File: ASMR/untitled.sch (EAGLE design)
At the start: 22 parts, among them J1 POWER_JACKSLT

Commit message: revisi PCB
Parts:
- added C3: 100nF, rcl:C-EUC0805K
- added R4: 10k, adafruit:R-US_M0805
- added S1: (no value), switch-omron:31-XX
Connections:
- new net RST: C3.1, R4.1, S1.S, U$6.IO0
- new net SCL: RTC1.SCL1, U$6.IO22
- new net SDA: RTC1.SDA1, U$6.IO21
- net GND: now also C3.2, RTC1.GND1, S1.P
- net INT_LAN: no longer U$6.IO22
- net OUT+: now also R4.2, RTC1.VCC1
- net RST_LAN: no longer U$6.IO21
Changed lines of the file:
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@@
 <part name="X2" library="con-molex" library_urn="urn:adsk.eagle:library:165" deviceset="KK-156-2" device="" package3d_urn="urn:adsk.eagle:package:8078800/1"/>
 <part name="RTC1" library="rtc3231" deviceset="RTC3231" device=""/>
+<part name="GND3" library="supply1" library_urn="urn:adsk.eagle:library:371" deviceset="GND" device=""/>
+<part name="S1" library="switch-omron" library_urn="urn:adsk.eagle:library:377" deviceset="31-XX" device="" package3d_urn="urn:adsk.eagle:package:27487/1"/>
+<part name="C3" library="rcl" library_urn="urn:adsk.eagle:library:334" deviceset="C-EU" device="C0805K" package3d_urn="urn:adsk.eagle:package:23681/2" value="100nF"/>
+<part name="R4" library="adafruit" library_urn="urn:adsk.eagle:library:420" deviceset="R-US_" device="M0805" package3d_urn="urn:adsk.eagle:package:6240587/1" value="10k"/>
 </parts>
 <sheets>
@@
 </instance>
 <instance part="RTC1" gate="G$1" x="88.9" y="35.56" smashed="yes"/>
+<instance part="GND3" gate="1" x="109.22" y="45.72" smashed="yes" rot="R180">
+<attribute name="VALUE" x="111.76" y="48.26" size="1.778" layer="96" rot="R180"/>
+</instance>
+<instance part="S1" gate="1" x="-104.14" y="30.48" smashed="yes" rot="R270">
+<attribute name="NAME" x="-106.045" y="36.83" size="1.778" layer="95"/>
+<attribute name="VALUE" x="-100.965" y="34.29" size="1.778" layer="96"/>
+</instance>
+<instance part="C3" gate="G$1" x="-101.6" y="27.94" smashed="yes" rot="R270">
+<attribute name="NAME" x="-101.219" y="26.416" size="1.778" layer="95" rot="R270"/>
+<attribute name="VALUE" x="-106.299" y="36.576" size="1.778" layer="96" rot="R270"/>
+</instance>
+<instance part="R4" gate="G$1" x="-96.52" y="40.64" smashed="yes" rot="R90">
+<attribute name="NAME" x="-98.0186" y="36.83" size="1.778" layer="95" rot="R90"/>
+<attribute name="VALUE" x="-93.218" y="36.83" size="1.778" layer="96" rot="R90"/>
+</instance>
 </instances>
 <busses>
@@
 <wire x1="-17.78" y1="30.48" x2="-17.78" y2="53.34" width="0.1524" layer="91"/>
 <wire x1="-17.78" y1="53.34" x2="-91.44" y2="53.34" width="0.1524" layer="91"/>
-<wire x1="-91.44" y1="53.34" x2="-91.44" y2="12.7" width="0.1524" layer="91"/>
+<wire x1="-91.44" y1="53.34" x2="-91.44" y2="25.4" width="0.1524" layer="91"/>
 <junction x="-91.44" y="12.7"/>
+<pinref part="S1" gate="1" pin="P"/>
+<wire x1="-91.44" y1="25.4" x2="-91.44" y2="12.7" width="0.1524" layer="91"/>
+<wire x1="-109.22" y1="30.48" x2="-111.76" y2="30.48" width="0.1524" layer="91"/>
+<wire x1="-111.76" y1="30.48" x2="-114.3" y2="30.48" width="0.1524" layer="91"/>
+<wire x1="-114.3" y1="30.48" x2="-114.3" y2="25.4" width="0.1524" layer="91"/>
+<wire x1="-91.44" y1="25.4" x2="-114.3" y2="25.4" width="0.1524" layer="91"/>
+<junction x="-91.44" y="25.4"/>
+<pinref part="C3" gate="G$1" pin="2"/>
+<wire x1="-106.68" y1="27.94" x2="-111.76" y2="27.94" width="0.1524" layer="91"/>
+<wire x1="-111.76" y1="27.94" x2="-111.76" y2="30.48" width="0.1524" layer="91"/>
+<junction x="-111.76" y="30.48"/>
 </segment>
 <segment>
@@
 <junction x="5.08" y="152.4"/>
 </segment>
+<segment>
+<pinref part="RTC1" gate="G$1" pin="GND1"/>
+<wire x1="104.14" y1="40.64" x2="109.22" y2="40.64" width="0.1524" layer="91"/>
+<wire x1="109.22" y1="40.64" x2="109.22" y2="43.18" width="0.1524" layer="91"/>
+<pinref part="GND3" gate="1" pin="GND"/>
+</segment>
 </net>
 <net name="3V3" class="0">
@@
 <label x="-81.28" y="-40.64" size="0.8128" layer="95" xref="yes"/>
 </segment>
-<segment>
-<pinref part="U$6" gate="G$1" pin="IO22"/>
-<wire x1="-68.58" y1="2.54" x2="-73.66" y2="2.54" width="0.1524" layer="91"/>
-<label x="-73.66" y="2.54" size="1.778" layer="95" rot="R180" xref="yes"/>
-</segment>
 </net>
 <net name="SCK_HSPI" class="0">
@@
 <wire x1="-114.3" y1="-43.18" x2="-119.38" y2="-43.18" width="0.1524" layer="91"/>
 <label x="-119.38" y="-43.18" size="0.8128" layer="95" rot="R180" xref="yes"/>
-</segment>
-<segment>
-<pinref part="U$6" gate="G$1" pin="IO21"/>
-<wire x1="-68.58" y1="10.16" x2="-73.66" y2="10.16" width="0.1524" layer="91"/>
-<label x="-73.66" y="10.16" size="1.778" layer="95" rot="R180" xref="yes"/>
 </segment>
 </net>
@@
 <label x="2.54" y="139.7" size="1.778" layer="95" xref="yes"/>
 </segment>
+<segment>
+<pinref part="RTC1" gate="G$1" pin="VCC1"/>
+<wire x1="104.14" y1="38.1" x2="119.38" y2="38.1" width="0.1524" layer="91"/>
+<wire x1="119.38" y1="38.1" x2="119.38" y2="40.64" width="0.1524" layer="91"/>
+<label x="119.38" y="40.64" size="1.778" layer="95" rot="R90" xref="yes"/>
+</segment>
+<segment>
+<pinref part="R4" gate="G$1" pin="2"/>
+<wire x1="-96.52" y1="45.72" x2="-96.52" y2="48.26" width="0.1524" layer="91"/>
+<label x="-96.52" y="48.26" size="1.778" layer="95" rot="R90" xref="yes"/>
+</segment>
 </net>
 <net name="N$2" class="0">
@@
 </segment>
 </net>
+<net name="SCL" class="0">
+<segment>
+<pinref part="U$6" gate="G$1" pin="IO22"/>
+<wire x1="-68.58" y1="2.54" x2="-73.66" y2="2.54" width="0.1524" layer="91"/>
+<label x="-73.66" y="2.54" size="1.778" layer="95" rot="R180" xref="yes"/>
+</segment>
+<segment>
+<pinref part="RTC1" gate="G$1" pin="SCL1"/>
+<wire x1="104.14" y1="33.02" x2="106.68" y2="33.02" width="0.1524" layer="91"/>
+<label x="106.68" y="33.02" size="1.778" layer="95" xref="yes"/>
+</segment>
+</net>
+<net name="SDA" class="0">
+<segment>
+<pinref part="U$6" gate="G$1" pin="IO21"/>
+<wire x1="-68.58" y1="10.16" x2="-73.66" y2="10.16" width="0.1524" layer="91"/>
+<label x="-73.66" y="10.16" size="1.778" layer="95" rot="R180" xref="yes"/>
+</segment>
+<segment>
+<pinref part="RTC1" gate="G$1" pin="SDA1"/>
+<wire x1="104.14" y1="35.56" x2="106.68" y2="35.56" width="0.1524" layer="91"/>
+<label x="106.68" y="35.56" size="1.778" layer="95" xref="yes"/>
+</segment>
+</net>
+<net name="RST" class="0">
+<segment>
+<pinref part="U$6" gate="G$1" pin="IO0"/>
+<label x="-73.66" y="30.48" size="1.778" layer="95" rot="R180" xref="yes"/>
+<pinref part="S1" gate="1" pin="S"/>
+<wire x1="-99.06" y1="30.48" x2="-96.52" y2="30.48" width="0.1524" layer="91"/>
+<pinref part="C3" gate="G$1" pin="1"/>
+<wire x1="-96.52" y1="30.48" x2="-68.58" y2="30.48" width="0.1524" layer="91"/>
+<wire x1="-99.06" y1="27.94" x2="-96.52" y2="27.94" width="0.1524" layer="91"/>
+<wire x1="-96.52" y1="27.94" x2="-96.52" y2="30.48" width="0.1524" layer="91"/>
+<junction x="-96.52" y="30.48"/>
+<pinref part="R4" gate="G$1" pin="1"/>
+<wire x1="-96.52" y1="30.48" x2="-96.52" y2="35.56" width="0.1524" layer="91"/>
+</segment>
+</net>

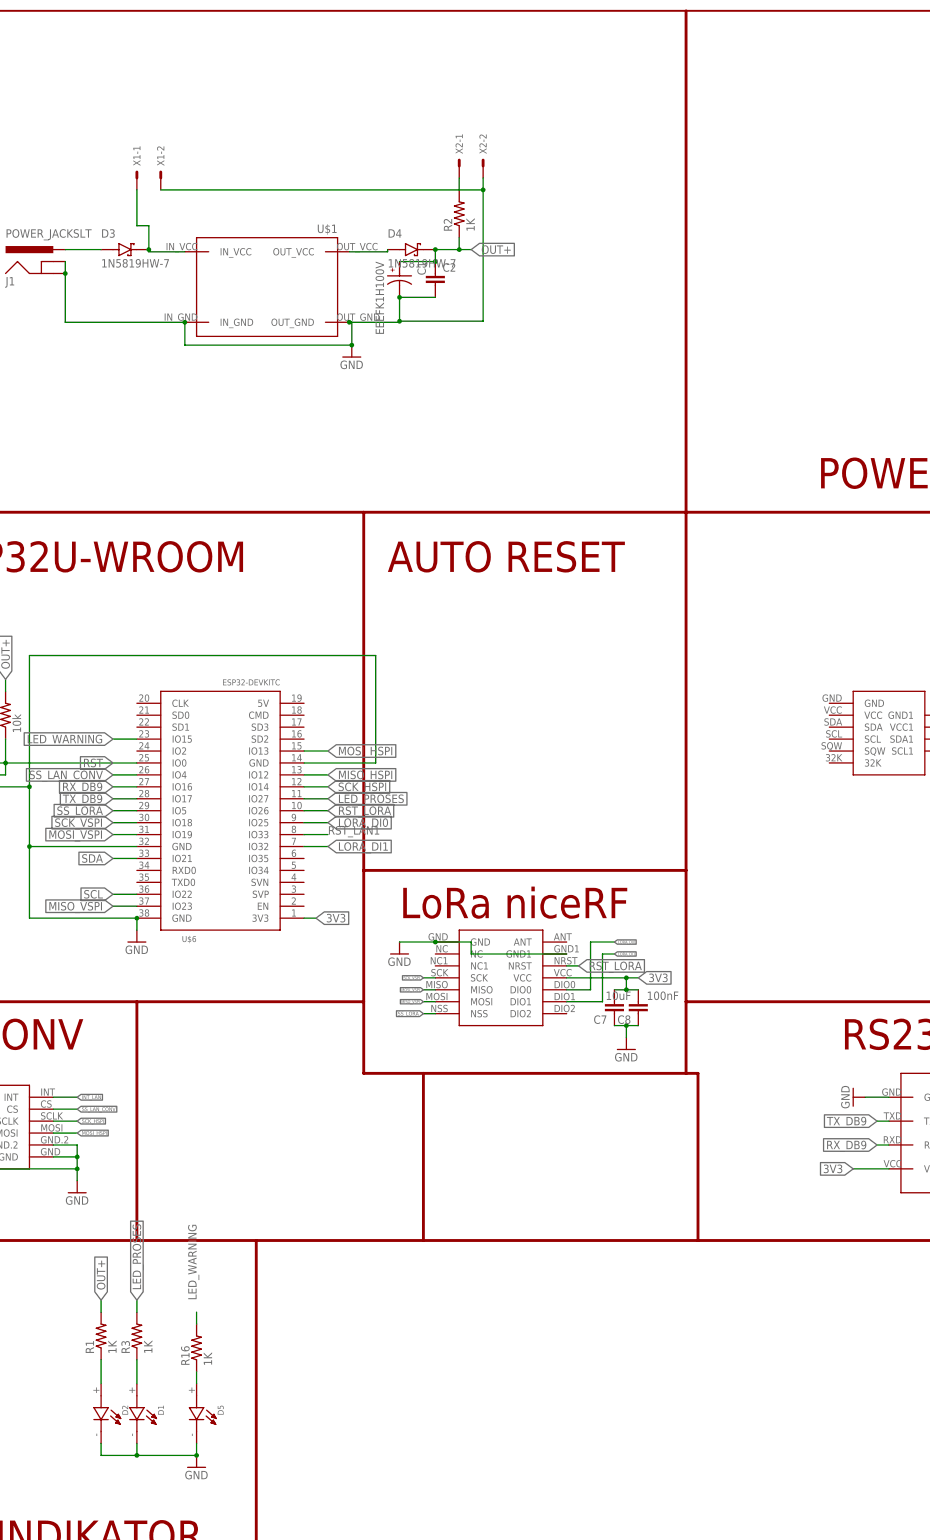
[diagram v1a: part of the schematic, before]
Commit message: pembuatan file .brd
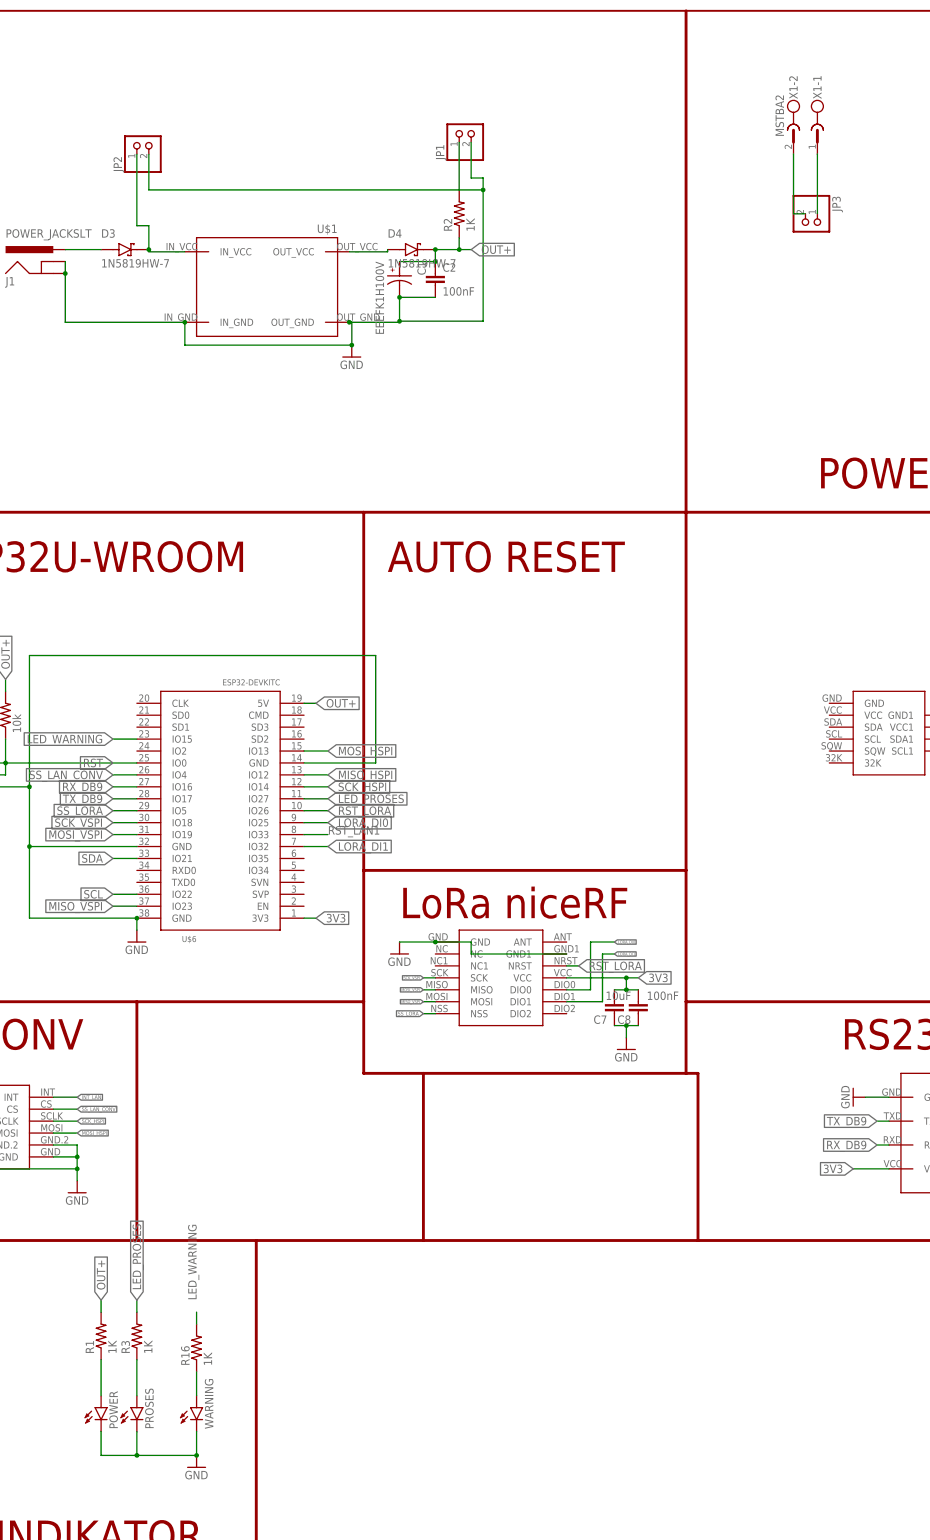
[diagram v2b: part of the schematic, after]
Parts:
- removed D1, D2: 3v3, LHN974_RED_LED_1206:LHN974_RED_LED_1206
- removed D5: 3v31, LHN974_RED_LED_1206:LHN974_RED_LED_1206
- removed X2: (no value), con-molex:KK-156-2
- added JP1, JP2, JP3: (no value), pinhead:PINHD-1X2
- added POWER, PROSES, WARNING: TLLR4400, led:TLLR4400
- C2: value (none) -> 100nF
- X1: value (none) -> MSTBA2; device con-molex:KK-156-2 -> con-phoenix-508:MSTBA2
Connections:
- new net N$5: JP3.2, X1-2.1
- new net N$8: JP3.1, X1-1.1
- net GND: now also JP1.2, JP2.2, POWER.C, PROSES.C, WARNING.C; no longer D1.-, D2.-, D5.-, X1-2.S, X2-2.S
- net N$1: now also POWER.A; no longer D2.+
- net N$16: now also WARNING.A; no longer D5.+
- net N$3: now also PROSES.A; no longer D1.+
- net N$4: now also JP2.1; no longer X1-1.S
- net N$7: now also JP1.1; no longer X2-1.S
- net OUT+: now also U$6.5V
